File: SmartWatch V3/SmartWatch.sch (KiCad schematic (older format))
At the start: 17 parts, among them J2 Bat_in, Q3 FDN340P, U1 S-13A1A33-E8T1U3, U2 LCD_TOUCH, U4 MAX9065, U5 MCP73811T-420I-OT, U7 ADXL337

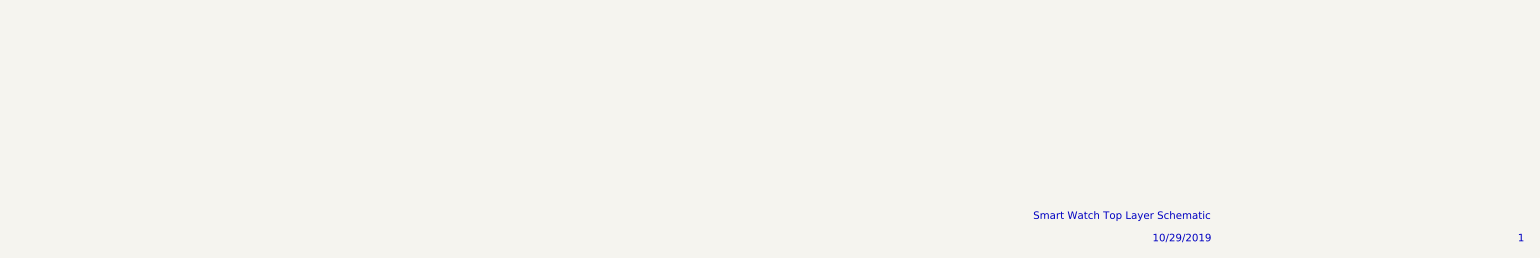
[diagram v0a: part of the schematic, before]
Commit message: Added notes to schematic for rev 4 changes
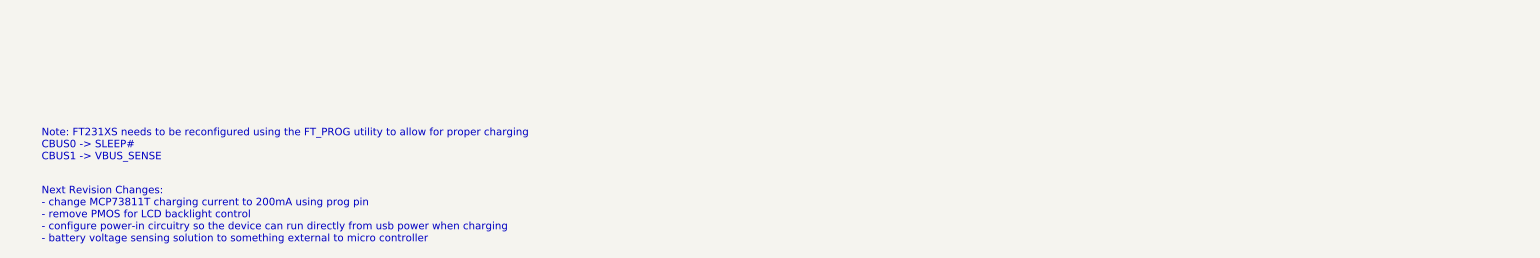
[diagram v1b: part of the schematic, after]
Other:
- note added: "Next Revision Changes: \n- change MCP73811T charging current to 200mA using prog pin\n- remove PMOS for LCD backlight control\n- configure power-in circuitry so the device can run directly from usb power when charging\n- battery voltage sensing solution to something external to micro controller\n"
- note added: "Note: FT231XS needs to be reconfigured using the FT_PROG utility to allow for proper charging\nCBUS0 -> SLEEP#\nCBUS1 -> VBUS_SENSE\n"
- note removed: "10/29/2019"
- note removed: "Smart Watch Top Layer Schematic"
- note removed: "\n1"
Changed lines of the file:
@@
 encoding utf-8
 Sheet 1 2
-Title ""
-Date ""
-Rev ""
+Title "ESP32 Smartwatch"
+Date "10/29/2019"
+Rev "3"
 Comp ""
 Comment1 ""
-Comment2 ""
-Comment3 ""
+Comment2 "https://hackaday.io/project/168227-custom-smartwatch"
+Comment3 "Offical project page can be found at "
 Comment4 ""
 $EndDescr
@@
 Z_SIG
 NoConn ~ 2950 3150
-Text Notes 7350 7500 0    50   ~ 0
-Smart Watch Top Layer Schematic
-Text Notes 10600 7650 0    50   ~ 0
-\n1
-Text Notes 8150 7650 0    50   ~ 0
-10/29/2019
 Wire Wire Line
 	5600 2500 6150 2500
@@
 	1    0    0    -1
 $EndComp
+Text Notes 700  7650 0    50   ~ 0
+Next Revision Changes: \n- change MCP73811T charging current to 200mA using prog pin\n- remove PMOS for LCD backlight control\n- configure power-in circuitry so the device can run directly from usb power when charging\n- battery voltage sensing solution to something external to micro controller\n
+Text Notes 700  7100 0    50   ~ 0
+Note: FT231XS needs to be reconfigured using the FT_PROG utility to allow for proper charging\nCBUS0 -> SLEEP#\nCBUS1 -> VBUS_SENSE\n
 $EndSCHEMATC
